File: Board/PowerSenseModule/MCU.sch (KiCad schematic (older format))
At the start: 38 parts, among them J3 Programming Header, J4 Conn_01x02_Male, U2 NCV2007x, U3 dsPIC33EV32GM102, U4 MCP2542FDxMF, Y1 25 MHz

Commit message: Changed crystal gnd net and working on layout
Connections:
- net GNDA: no longer C17.2, C18.2, Y1.2
- net GNDD: now also C17.2, C18.2, Y1.2
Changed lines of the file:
@@
 	0    -1   -1   0
 $EndComp
-$Comp
-L power:GNDA #PWR035
-U 1 1 5D9832AA
-P 5070 5370
-F 0 "#PWR035" H 5070 5120 50  0001 C CNN
-F 1 "GNDA" V 5075 5242 50  0000 R CNN
-F 2 "" H 5070 5370 50  0001 C CNN
-F 3 "" H 5070 5370 50  0001 C CNN
-	1    5070 5370
-	0    -1   -1   0
-$EndComp
-Wire Wire Line
-	5070 5200 5070 5370
-Connection ~ 5070 5370
-Wire Wire Line
-	5070 5370 5070 5550
 Wire Wire Line
 	4775 5550 4770 5550
@@
 Wire Wire Line
 	3275 1400 3275 1500
-$Comp
-L power:GNDA #PWR0107
-U 1 1 5DFA3DB1
+Text Notes 4050 6200 0    50   ~ 0
+both pins 2 and 4 are connected to\nthe lid, so only need to connect one to\nground. After PCB layout, easier to connect\nonly pin 2.
+NoConn ~ 4300 5375
+Wire Wire Line
+	4500 5375 4525 5375
+Wire Wire Line
+	4525 5625 4525 5375
+$Comp
+L power:GNDD #PWR0107
+U 1 1 5DF77780
 P 4525 5625
 F 0 "#PWR0107" H 4525 5375 50  0001 C CNN
-F 1 "GNDA" H 4530 5452 50  0000 C CNN
+F 1 "GNDD" H 4529 5470 50  0000 C CNN
 F 2 "" H 4525 5625 50  0001 C CNN
 F 3 "" H 4525 5625 50  0001 C CNN
@@
 	1    0    0    -1
 $EndComp
-Text Notes 4050 6200 0    50   ~ 0
-both pins 2 and 4 are connected to\nthe lid, so only need to connect one to\nground. After PCB layout, easier to connect\nonly pin 2.
-NoConn ~ 4300 5375
-Wire Wire Line
-	4500 5375 4525 5375
-Wire Wire Line
-	4525 5625 4525 5375
+Wire Wire Line
+	5070 5200 5070 5350
+Wire Wire Line
+	5070 5350 5300 5350
+Wire Wire Line
+	5300 5350 5300 5625
+$Comp
+L power:GNDD #PWR?
+U 1 1 5DF81099
+P 5300 5625
+F 0 "#PWR?" H 5300 5375 50  0001 C CNN
+F 1 "GNDD" H 5304 5470 50  0000 C CNN
+F 2 "" H 5300 5625 50  0001 C CNN
+F 3 "" H 5300 5625 50  0001 C CNN
+	1    5300 5625
+	1    0    0    -1
+$EndComp
+Connection ~ 5070 5350
+Wire Wire Line
+	5070 5350 5070 5550
 $EndSCHEMATC

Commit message: layout 0.01
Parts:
- added C24: 0.01uF, Capacitor_SMD:C_0603_1608Metric_Pad1.05x0.95mm_HandSolder, symbol Device:C
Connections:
- net GNDA: now also C24.2
- net VS: now also C24.1
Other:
- moved on the sheet: U2E
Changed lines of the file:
@@
 L F1_OP_Amps:NCV2007x U2
 U 5 1 5D4B8129
-P 5725 7075
-F 0 "U2" H 5803 7146 50  0000 L CNN
-F 1 "NCV2007x" H 5803 7055 50  0000 L CNN
-F 2 "Package_SO:TSSOP-14_4.4x5mm_P0.65mm" H 5725 6725 50  0001 C CNN
-F 3 "https://www.onsemi.com/pub/Collateral/NCS20071-D.PDF" H 5725 6725 50  0001 C CNN
-F 4 "ON Semiconductor" H 5725 7075 50  0001 C CNN "Manufacturer"
-F 5 "NCV20074DR2G " H 5725 7075 50  0001 C CNN "Manufacturer PN"
-F 6 "Mouser" H 5725 7075 50  0001 C CNN "Supplier"
-F 7 "https://www.mouser.com/ProductDetail/ON-Semiconductor/NCV20074DR2G?qs=sGAEpiMZZMtCHixnSjNA6NXlPpRsFEjtp%252BTBls3ALHY%3D" H 5725 7075 50  0001 C CNN "Supplier Link"
-F 8 " 863-NCV20074DR2G " H 5725 7075 50  0001 C CNN "Supplier PN"
-F 9 "1.19" H 5725 7075 50  0001 C CNN "Price 1 QTY"
-	5    5725 7075
+P 5195 7035
+F 0 "U2" H 5273 7106 50  0000 L CNN
+F 1 "NCV2007x" H 5273 7015 50  0000 L CNN
+F 2 "Package_SO:TSSOP-14_4.4x5mm_P0.65mm" H 5195 6685 50  0001 C CNN
+F 3 "https://www.onsemi.com/pub/Collateral/NCS20071-D.PDF" H 5195 6685 50  0001 C CNN
+F 4 "ON Semiconductor" H 5195 7035 50  0001 C CNN "Manufacturer"
+F 5 "NCV20074DR2G " H 5195 7035 50  0001 C CNN "Manufacturer PN"
+F 6 "Mouser" H 5195 7035 50  0001 C CNN "Supplier"
+F 7 "https://www.mouser.com/ProductDetail/ON-Semiconductor/NCV20074DR2G?qs=sGAEpiMZZMtCHixnSjNA6NXlPpRsFEjtp%252BTBls3ALHY%3D" H 5195 7035 50  0001 C CNN "Supplier Link"
+F 8 " 863-NCV20074DR2G " H 5195 7035 50  0001 C CNN "Supplier PN"
+F 9 "1.19" H 5195 7035 50  0001 C CNN "Price 1 QTY"
+	5    5195 7035
 	1    0    0    -1
 $EndComp
@@
 L power:GNDA #PWR011
 U 1 1 5D527CAD
-P 5725 7375
-F 0 "#PWR011" H 5725 7125 50  0001 C CNN
-F 1 "GNDA" H 5730 7202 50  0000 C CNN
-F 2 "" H 5725 7375 50  0001 C CNN
-F 3 "" H 5725 7375 50  0001 C CNN
-	1    5725 7375
+P 5195 7335
+F 0 "#PWR011" H 5195 7085 50  0001 C CNN
+F 1 "GNDA" H 5200 7162 50  0000 C CNN
+F 2 "" H 5195 7335 50  0001 C CNN
+F 3 "" H 5195 7335 50  0001 C CNN
+	1    5195 7335
 	1    0    0    -1
 $EndComp
@@
 L power:VS #PWR036
 U 1 1 5E3CF0BD
-P 5725 6725
-F 0 "#PWR036" H 5525 6575 50  0001 C CNN
-F 1 "VS" H 5742 6898 50  0000 C CNN
-F 2 "" H 5725 6725 50  0001 C CNN
-F 3 "" H 5725 6725 50  0001 C CNN
-	1    5725 6725
+P 5195 6685
+F 0 "#PWR036" H 4995 6535 50  0001 C CNN
+F 1 "VS" H 5212 6858 50  0000 C CNN
+F 2 "" H 5195 6685 50  0001 C CNN
+F 3 "" H 5195 6685 50  0001 C CNN
+	1    5195 6685
 	1    0    0    -1
 $EndComp
@@
 	5300 5350 5300 5625
 $Comp
-L power:GNDD #PWR?
+L power:GNDD #PWR0109
 U 1 1 5DF81099
 P 5300 5625
-F 0 "#PWR?" H 5300 5375 50  0001 C CNN
+F 0 "#PWR0109" H 5300 5375 50  0001 C CNN
 F 1 "GNDD" H 5304 5470 50  0000 C CNN
 F 2 "" H 5300 5625 50  0001 C CNN
@@
 Wire Wire Line
 	5070 5350 5070 5550
+$Comp
+L Device:C C24
+U 1 1 5DFD1FA1
+P 6040 7040
+F 0 "C24" H 6155 7086 50  0000 L CNN
+F 1 "0.01uF" H 6155 6995 50  0000 L CNN
+F 2 "Capacitor_SMD:C_0603_1608Metric_Pad1.05x0.95mm_HandSolder" H 6078 6890 50  0001 C CNN
+F 3 "~" H 6040 7040 50  0001 C CNN
+	1    6040 7040
+	1    0    0    -1
+$EndComp
+$Comp
+L power:GNDA #PWR038
+U 1 1 5DFE653F
+P 6040 7190
+F 0 "#PWR038" H 6040 6940 50  0001 C CNN
+F 1 "GNDA" H 6045 7017 50  0000 C CNN
+F 2 "" H 6040 7190 50  0001 C CNN
+F 3 "" H 6040 7190 50  0001 C CNN
+	1    6040 7190
+	1    0    0    -1
+$EndComp
+$Comp
+L power:VS #PWR035
+U 1 1 5DFEFB45
+P 6040 6890
+F 0 "#PWR035" H 5840 6740 50  0001 C CNN
+F 1 "VS" H 6057 7063 50  0000 C CNN
+F 2 "" H 6040 6890 50  0001 C CNN
+F 3 "" H 6040 6890 50  0001 C CNN
+	1    6040 6890
+	1    0    0    -1
+$EndComp
 $EndSCHEMATC

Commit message: layout 0.04
- Added top and bottom ground plane
- changed GNDD to GND
- readjusted spacing between components
- made the board a little smaller
- fine tuned copper fills
- got pretty good power rail and ground layout
- length matched traces from sense resistor to op amp
- repositioned LEDs
- added text for LEDs

TODO:
- maybe reorganize passives between MCU and op amps
- layout/route the three resistors for the op amps currently on the bottom of the PCB
- move shunt resistor for CAN closer to connector (?)
- route length tuned traces for CANH and CANL
- GNDA copper fills
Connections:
- net GNDD renamed GND
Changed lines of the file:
@@
-	1    0    0    -1
-$EndComp
-$Comp
-L power:GNDD #PWR031
-U 1 1 5D3FDEC2
-P 1625 5800
-F 0 "#PWR031" H 1625 5550 50  0001 C CNN
-F 1 "GNDD" H 1625 5650 50  0000 C CNN
-F 2 "" H 1625 5800 50  0001 C CNN
-F 3 "" H 1625 5800 50  0001 C CNN
-	1    1625 5800
-	1    0    0    -1
-$EndComp
-$Comp
-L power:GNDD #PWR016
-U 1 1 5D3FB889
-P 1250 7125
-F 0 "#PWR016" H 1250 6875 50  0001 C CNN
-F 1 "GNDD" H 1254 6970 50  0000 C CNN
-F 2 "" H 1250 7125 50  0001 C CNN
-F 3 "" H 1250 7125 50  0001 C CNN
-	1    1250 7125
-	1    0    0    -1
-$EndComp
-$Comp
-L power:GNDD #PWR020
-U 1 1 5D3FABB0
-P 3400 7200
-F 0 "#PWR020" H 3400 6950 50  0001 C CNN
-F 1 "GNDD" H 3404 7045 50  0000 C CNN
-F 2 "" H 3400 7200 50  0001 C CNN
-F 3 "" H 3400 7200 50  0001 C CNN
-	1    3400 7200
-	1    0    0    -1
-$EndComp
-$Comp
-L power:GNDD #PWR028
-U 1 1 5D3C46D6
-P 7075 5800
-F 0 "#PWR028" H 7075 5550 50  0001 C CNN
-F 1 "GNDD" H 7079 5645 50  0000 C CNN
-F 2 "" H 7075 5800 50  0001 C CNN
-F 3 "" H 7075 5800 50  0001 C CNN
-	1    7075 5800
 	1    0    0    -1
 $EndComp
@@
 Wire Wire Line
 	9850 5150 9650 5150
-$Comp
-L power:GNDD #PWR0106
-U 1 1 5D597A06
-P 10450 5250
-F 0 "#PWR0106" H 10450 5000 50  0001 C CNN
-F 1 "GNDD" H 10454 5095 50  0000 C CNN
-F 2 "" H 10450 5250 50  0001 C CNN
-F 3 "" H 10450 5250 50  0001 C CNN
-	1    10450 5250
-	1    0    0    -1
-$EndComp
 Wire Wire Line
 	10050 5575 10350 5575
@@
 Wire Wire Line
 	9250 5575 9125 5575
-$Comp
-L power:GNDD #PWR037
-U 1 1 5E0DEE0A
-P 10350 5725
-F 0 "#PWR037" H 10350 5475 50  0001 C CNN
-F 1 "GNDD" H 10354 5570 50  0000 C CNN
-F 2 "" H 10350 5725 50  0001 C CNN
-F 3 "" H 10350 5725 50  0001 C CNN
-	1    10350 5725
-	1    0    0    -1
-$EndComp
 Wire Wire Line
 	10350 5725 10350 5575
@@
 	1425 2200 1425 2230
 $Comp
-L power:GNDD #PWR0105
-U 1 1 5D4D1DB2
-P 4525 4125
-F 0 "#PWR0105" H 4525 3875 50  0001 C CNN
-F 1 "GNDD" H 4529 3970 50  0000 C CNN
-F 2 "" H 4525 4125 50  0001 C CNN
-F 3 "" H 4525 4125 50  0001 C CNN
-	1    4525 4125
-	1    0    0    -1
-$EndComp
-$Comp
 L Device:C C12
 U 1 1 5D1BA03E
@@
 Only one soldered\n
 $Comp
-L power:GNDD #PWR033
-U 1 1 5D53513F
-P 5250 2375
-F 0 "#PWR033" H 5250 2125 50  0001 C CNN
-F 1 "GNDD" H 5254 2220 50  0000 C CNN
-F 2 "" H 5250 2375 50  0001 C CNN
-F 3 "" H 5250 2375 50  0001 C CNN
-	1    5250 2375
-	1    0    0    -1
-$EndComp
-$Comp
 L Device:R_Small_US R16
 U 1 1 5D52A243
@@
 Wire Wire Line
 	2825 4150 2825 4350
-$Comp
-L power:GNDA #PWR024
-U 1 1 5D516C00
-P 2825 4350
-F 0 "#PWR024" H 2825 4100 50  0001 C CNN
-F 1 "GNDA" H 2830 4177 50  0000 C CNN
-F 2 "" H 2825 4350 50  0001 C CNN
-F 3 "" H 2825 4350 50  0001 C CNN
-	1    2825 4350
-	1    0    0    -1
-$EndComp
-$Comp
-L power:GNDD #PWR026
-U 1 1 5D514FF2
-P 3125 4350
-F 0 "#PWR026" H 3125 4100 50  0001 C CNN
-F 1 "GNDD" H 3129 4195 50  0000 C CNN
-F 2 "" H 3125 4350 50  0001 C CNN
-F 3 "" H 3125 4350 50  0001 C CNN
-	1    3125 4350
-	1    0    0    -1
-$EndComp
 $Comp
 L Device:CP1 C15
@@
 Wire Wire Line
 	3125 1300 3125 1500
-$Comp
-L power:GNDD #PWR025
-U 1 1 5D3FBC0D
-P 3675 1100
-F 0 "#PWR025" H 3675 850 50  0001 C CNN
-F 1 "GNDD" H 3679 945 50  0000 C CNN
-F 2 "" H 3675 1100 50  0001 C CNN
-F 3 "" H 3675 1100 50  0001 C CNN
-	1    3675 1100
-	1    0    0    -1
-$EndComp
-$Comp
-L power:GNDD #PWR018
-U 1 1 5D3FC142
-P 1425 2530
-F 0 "#PWR018" H 1425 2280 50  0001 C CNN
-F 1 "GNDD" H 1429 2375 50  0000 C CNN
-F 2 "" H 1425 2530 50  0001 C CNN
-F 3 "" H 1425 2530 50  0001 C CNN
-	1    1425 2530
-	1    0    0    -1
-$EndComp
 Wire Wire Line
 	1925 1900 1875 1900
@@
 Wire Wire Line
 	4525 5625 4525 5375
-$Comp
-L power:GNDD #PWR0107
-U 1 1 5DF77780
-P 4525 5625
-F 0 "#PWR0107" H 4525 5375 50  0001 C CNN
-F 1 "GNDD" H 4529 5470 50  0000 C CNN
-F 2 "" H 4525 5625 50  0001 C CNN
-F 3 "" H 4525 5625 50  0001 C CNN
-	1    4525 5625
-	1    0    0    -1
-$EndComp
 Wire Wire Line
 	5070 5200 5070 5350
@@
 Wire Wire Line
 	5300 5350 5300 5625
-$Comp
-L power:GNDD #PWR0109
-U 1 1 5DF81099
-P 5300 5625
-F 0 "#PWR0109" H 5300 5375 50  0001 C CNN
-F 1 "GNDD" H 5304 5470 50  0000 C CNN
-F 2 "" H 5300 5625 50  0001 C CNN
-F 3 "" H 5300 5625 50  0001 C CNN
-	1    5300 5625
-	1    0    0    -1
-$EndComp
 Connection ~ 5070 5350
 Wire Wire Line
@@
 	1    0    0    -1
 $EndComp
+$Comp
+L power:GND #PWR029
+U 1 1 5DF48E36
+P 4525 4125
+F 0 "#PWR029" H 4525 3875 50  0001 C CNN
+F 1 "GND" H 4530 3952 50  0000 C CNN
+F 2 "" H 4525 4125 50  0001 C CNN
+F 3 "" H 4525 4125 50  0001 C CNN
+	1    4525 4125
+	1    0    0    -1
+$EndComp
+$Comp
+L power:GNDA #PWR024
+U 1 1 5D516C00
+P 2825 4350
+F 0 "#PWR024" H 2825 4100 50  0001 C CNN
+F 1 "GNDA" H 2830 4177 50  0000 C CNN
+F 2 "" H 2825 4350 50  0001 C CNN
+F 3 "" H 2825 4350 50  0001 C CNN
+	1    2825 4350
+	1    0    0    -1
+$EndComp
+$Comp
+L power:GND #PWR026
+U 1 1 5DF4B387
+P 3125 4350
+F 0 "#PWR026" H 3125 4100 50  0001 C CNN
+F 1 "GND" H 3130 4177 50  0000 C CNN
+F 2 "" H 3125 4350 50  0001 C CNN
+F 3 "" H 3125 4350 50  0001 C CNN
+	1    3125 4350
+	1    0    0    -1
+$EndComp
+$Comp
+L power:GND #PWR022
+U 1 1 5DF4BBB3
+P 1425 2530
+F 0 "#PWR022" H 1425 2280 50  0001 C CNN
+F 1 "GND" H 1430 2357 50  0000 C CNN
+F 2 "" H 1425 2530 50  0001 C CNN
+F 3 "" H 1425 2530 50  0001 C CNN
+	1    1425 2530
+	1    0    0    -1
+$EndComp
+$Comp
+L power:GND #PWR028
+U 1 1 5DF4C5A9
+P 3675 1100
+F 0 "#PWR028" H 3675 850 50  0001 C CNN
+F 1 "GND" H 3680 927 50  0000 C CNN
+F 2 "" H 3675 1100 50  0001 C CNN
+F 3 "" H 3675 1100 50  0001 C CNN
+	1    3675 1100
+	1    0    0    -1
+$EndComp
+$Comp
+L power:GND #PWR033
+U 1 1 5DF4D23A
+P 5250 2375
+F 0 "#PWR033" H 5250 2125 50  0001 C CNN
+F 1 "GND" H 5255 2202 50  0000 C CNN
+F 2 "" H 5250 2375 50  0001 C CNN
+F 3 "" H 5250 2375 50  0001 C CNN
+	1    5250 2375
+	1    0    0    -1
+$EndComp
+$Comp
+L power:GND #PWR025
+U 1 1 5DF4DE04
+P 1625 5800
+F 0 "#PWR025" H 1625 5550 50  0001 C CNN
+F 1 "GND" H 1630 5627 50  0000 C CNN
+F 2 "" H 1625 5800 50  0001 C CNN
+F 3 "" H 1625 5800 50  0001 C CNN
+	1    1625 5800
+	1    0    0    -1
+$EndComp
+$Comp
+L power:GND #PWR020
+U 1 1 5DF4EB03
+P 1250 7125
+F 0 "#PWR020" H 1250 6875 50  0001 C CNN
+F 1 "GND" H 1255 6952 50  0000 C CNN
+F 2 "" H 1250 7125 50  0001 C CNN
+F 3 "" H 1250 7125 50  0001 C CNN
+	1    1250 7125
+	1    0    0    -1
+$EndComp
+$Comp
+L power:GND #PWR027
+U 1 1 5DF4F314
+P 3400 7200
+F 0 "#PWR027" H 3400 6950 50  0001 C CNN
+F 1 "GND" H 3405 7027 50  0000 C CNN
+F 2 "" H 3400 7200 50  0001 C CNN
+F 3 "" H 3400 7200 50  0001 C CNN
+	1    3400 7200
+	1    0    0    -1
+$EndComp
+$Comp
+L power:GND #PWR031
+U 1 1 5DF4FC98
+P 4525 5625
+F 0 "#PWR031" H 4525 5375 50  0001 C CNN
+F 1 "GND" H 4530 5452 50  0000 C CNN
+F 2 "" H 4525 5625 50  0001 C CNN
+F 3 "" H 4525 5625 50  0001 C CNN
+	1    4525 5625
+	1    0    0    -1
+$EndComp
+$Comp
+L power:GND #PWR037
+U 1 1 5DF5066C
+P 5300 5625
+F 0 "#PWR037" H 5300 5375 50  0001 C CNN
+F 1 "GND" H 5305 5452 50  0000 C CNN
+F 2 "" H 5300 5625 50  0001 C CNN
+F 3 "" H 5300 5625 50  0001 C CNN
+	1    5300 5625
+	1    0    0    -1
+$EndComp
+$Comp
+L power:GND #PWR039
+U 1 1 5DF510E8
+P 7075 5800
+F 0 "#PWR039" H 7075 5550 50  0001 C CNN
+F 1 "GND" H 7080 5627 50  0000 C CNN
+F 2 "" H 7075 5800 50  0001 C CNN
+F 3 "" H 7075 5800 50  0001 C CNN
+	1    7075 5800
+	1    0    0    -1
+$EndComp
+$Comp
+L power:GND #PWR040
+U 1 1 5DF526B8
+P 10350 5725
+F 0 "#PWR040" H 10350 5475 50  0001 C CNN
+F 1 "GND" H 10355 5552 50  0000 C CNN
+F 2 "" H 10350 5725 50  0001 C CNN
+F 3 "" H 10350 5725 50  0001 C CNN
+	1    10350 5725
+	1    0    0    -1
+$EndComp
+$Comp
+L power:GND #PWR041
+U 1 1 5DF53141
+P 10450 5250
+F 0 "#PWR041" H 10450 5000 50  0001 C CNN
+F 1 "GND" H 10455 5077 50  0000 C CNN
+F 2 "" H 10450 5250 50  0001 C CNN
+F 3 "" H 10450 5250 50  0001 C CNN
+	1    10450 5250
+	1    0    0    -1
+$EndComp

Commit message: layout 0.05
- differential pair for CAN bus
- differential pair for shunt resistor
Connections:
- net SENSE+: now reaches J4.1 (Pin_1), R6.2, R8.1, U2.3 (+)
- net SENSE-: now reaches J4.2 (Pin_2), R8.2, R9.1, U2.5 (+)
- net CANH renamed CAN+
- net CANL renamed CAN-
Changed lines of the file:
@@
 	7075 5375 7075 5675
 Text HLabel 2700 5550 2    50   Input ~ 0
-CANL
+CAN-
 Text HLabel 2700 5250 2    50   Input ~ 0
-CANH
+CAN+
 Wire Wire Line
 	7075 5275 7075 5025
@@
 	1    0    0    -1
 $EndComp
+Text Label 7320 1750 0    50   ~ 0
+SENSE+
+Text Label 7330 2250 0    50   ~ 0
+SENSE-
 $EndSCHEMATC

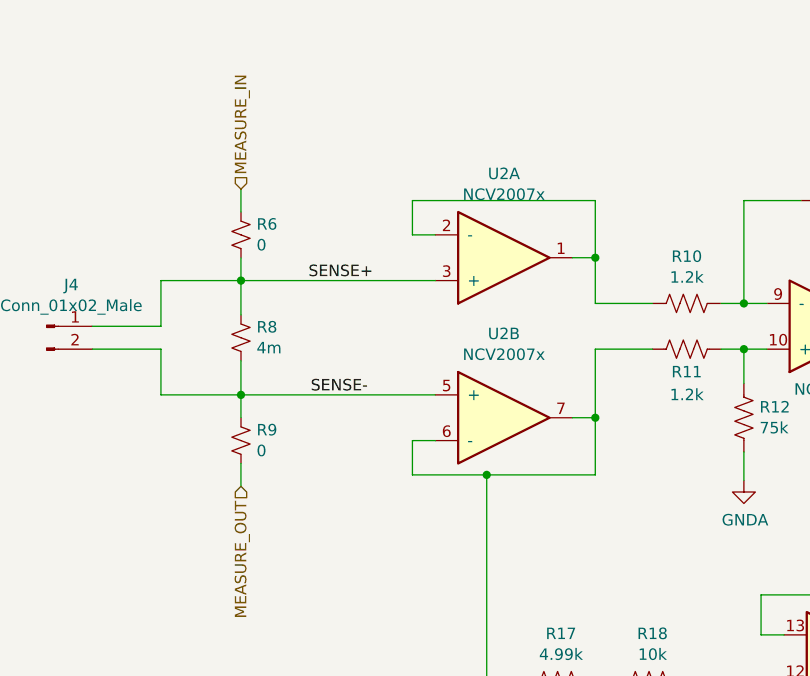
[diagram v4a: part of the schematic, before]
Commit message: layout 0.06
- finished most of the routing

TODO
- deal with copper island
- route GNDA
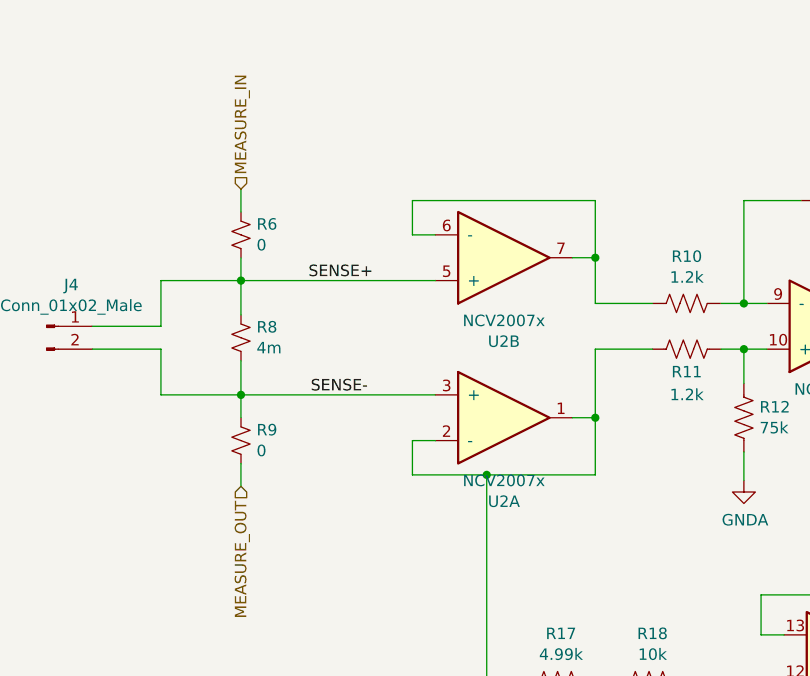
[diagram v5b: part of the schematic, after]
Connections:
- net SENSE+: now also U2.5 (+); no longer U2.3 (+)
- net SENSE-: now also U2.3 (+); no longer U2.5 (+)
- net at U2.1, U2.2 (-): now also R11.2, R17.2; no longer R10.2
- net at U2.6 (-), U2.7: now also R10.2; no longer R11.2, R17.2
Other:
- moved on the sheet: U2A, U2B
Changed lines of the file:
@@
 Wire Wire Line
 	7775 2600 8100 2600
-Wire Wire Line
-	7775 2450 7775 2600
-Wire Wire Line
-	7875 2450 7775 2450
-Wire Wire Line
-	7875 2250 7025 2250
 $Comp
 L F1_OP_Amps:NCV2007x U2
@@
 L F1_OP_Amps:NCV2007x U2
 U 2 1 5D4B605F
+P 8125 1650
+F 0 "U2" H 8175 2017 50  0000 C CNN
+F 1 "NCV2007x" H 8175 1926 50  0000 C CNN
+F 2 "Package_SO:TSSOP-14_4.4x5mm_P0.65mm" H 8125 1300 50  0001 C CNN
+F 3 "https://www.onsemi.com/pub/Collateral/NCS20071-D.PDF" H 8125 1300 50  0001 C CNN
+F 4 "ON Semiconductor" H 8125 1650 50  0001 C CNN "Manufacturer"
+F 5 "NCV20074DR2G " H 8125 1650 50  0001 C CNN "Manufacturer PN"
+F 6 "Mouser" H 8125 1650 50  0001 C CNN "Supplier"
+F 7 "https://www.mouser.com/ProductDetail/ON-Semiconductor/NCV20074DR2G?qs=sGAEpiMZZMtCHixnSjNA6NXlPpRsFEjtp%252BTBls3ALHY%3D" H 8125 1650 50  0001 C CNN "Supplier Link"
+F 8 " 863-NCV20074DR2G " H 8125 1650 50  0001 C CNN "Supplier PN"
+F 9 "1.19" H 8125 1650 50  0001 C CNN "Price 1 QTY"
+	2    8125 1650
+	1    0    0    1
+$EndComp
+$Comp
+L F1_OP_Amps:NCV2007x U2
+U 1 1 5D4B495F
 P 8125 2350
-F 0 "U2" H 8175 2717 50  0000 C CNN
-F 1 "NCV2007x" H 8175 2626 50  0000 C CNN
+F 0 "U2" H 8175 1983 50  0000 C CNN
+F 1 "NCV2007x" H 8175 2074 50  0000 C CNN
 F 2 "Package_SO:TSSOP-14_4.4x5mm_P0.65mm" H 8125 2000 50  0001 C CNN
 F 3 "https://www.onsemi.com/pub/Collateral/NCS20071-D.PDF" H 8125 2000 50  0001 C CNN
@@
 F 8 " 863-NCV20074DR2G " H 8125 2350 50  0001 C CNN "Supplier PN"
 F 9 "1.19" H 8125 2350 50  0001 C CNN "Price 1 QTY"
-	2    8125 2350
-	1    0    0    -1
-$EndComp
-$Comp
-L F1_OP_Amps:NCV2007x U2
-U 1 1 5D4B495F
-P 8125 1650
-F 0 "U2" H 8175 1283 50  0000 C CNN
-F 1 "NCV2007x" H 8175 1374 50  0000 C CNN
-F 2 "Package_SO:TSSOP-14_4.4x5mm_P0.65mm" H 8125 1300 50  0001 C CNN
-F 3 "https://www.onsemi.com/pub/Collateral/NCS20071-D.PDF" H 8125 1300 50  0001 C CNN
-F 4 "ON Semiconductor" H 8125 1650 50  0001 C CNN "Manufacturer"
-F 5 "NCV20074DR2G " H 8125 1650 50  0001 C CNN "Manufacturer PN"
-F 6 "Mouser" H 8125 1650 50  0001 C CNN "Supplier"
-F 7 "https://www.mouser.com/ProductDetail/ON-Semiconductor/NCV20074DR2G?qs=sGAEpiMZZMtCHixnSjNA6NXlPpRsFEjtp%252BTBls3ALHY%3D" H 8125 1650 50  0001 C CNN "Supplier Link"
-F 8 " 863-NCV20074DR2G " H 8125 1650 50  0001 C CNN "Supplier PN"
-F 9 "1.19" H 8125 1650 50  0001 C CNN "Price 1 QTY"
-	1    8125 1650
-	1    0    0    1
+	1    8125 2350
+	1    0    0    -1
 $EndComp
 Wire Wire Line
@@
 Text Label 7330 2250 0    50   ~ 0
 SENSE-
+Wire Wire Line
+	7025 2250 7875 2250
+Wire Wire Line
+	7775 2600 7775 2450
+Wire Wire Line
+	7775 2450 7875 2450
 $EndSCHEMATC
